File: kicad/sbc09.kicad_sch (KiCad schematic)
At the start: 78 parts, among them J1 Conn_01x03_Male, J2 Conn_01x06_Male, J3 Conn_01x06_Male, J4 Conn_01x06_Male, J5 Conn_02x05_Odd_Even, J6 Conn_02x25_Odd_Even, Q1 2N7000, SW1 SW_Push, U1 74LS245, U10 74LS670, U11 74LS670, U12 AS6C4008-55PCN, U13 SST39SF040-DIP, U14 SST39SF040-DIP, U15 XR68C681CJ, U16 MAX232, U2 74LS245, U3 74LS245, U4 MC6809E, U5 74HCT125, U6 ATF22V10C, U7 ATF22V10C, U8 74LS670, U9 74LS670, X1 8MHz, X2 3.6864MHz

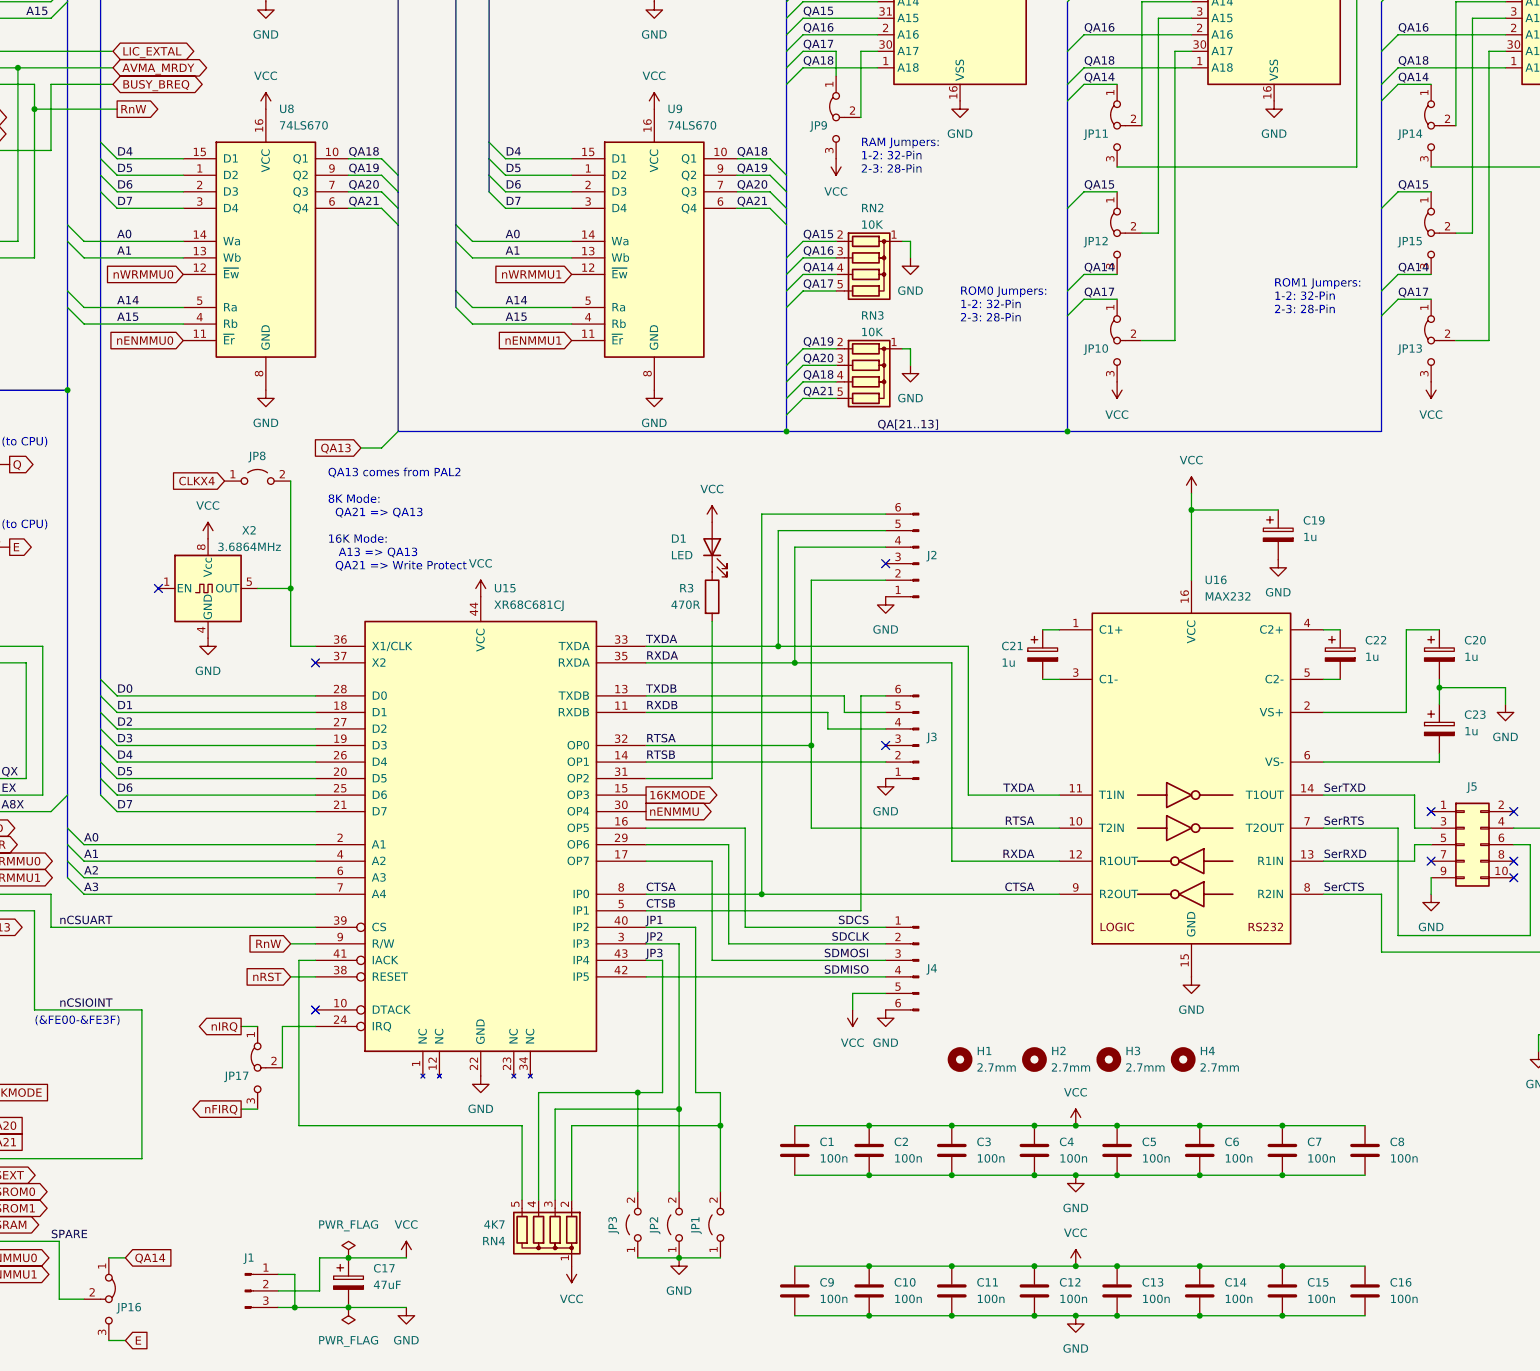
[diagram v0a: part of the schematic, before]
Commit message: Remove JP8 (caused fast clock stub) and renumbered remaining JPs
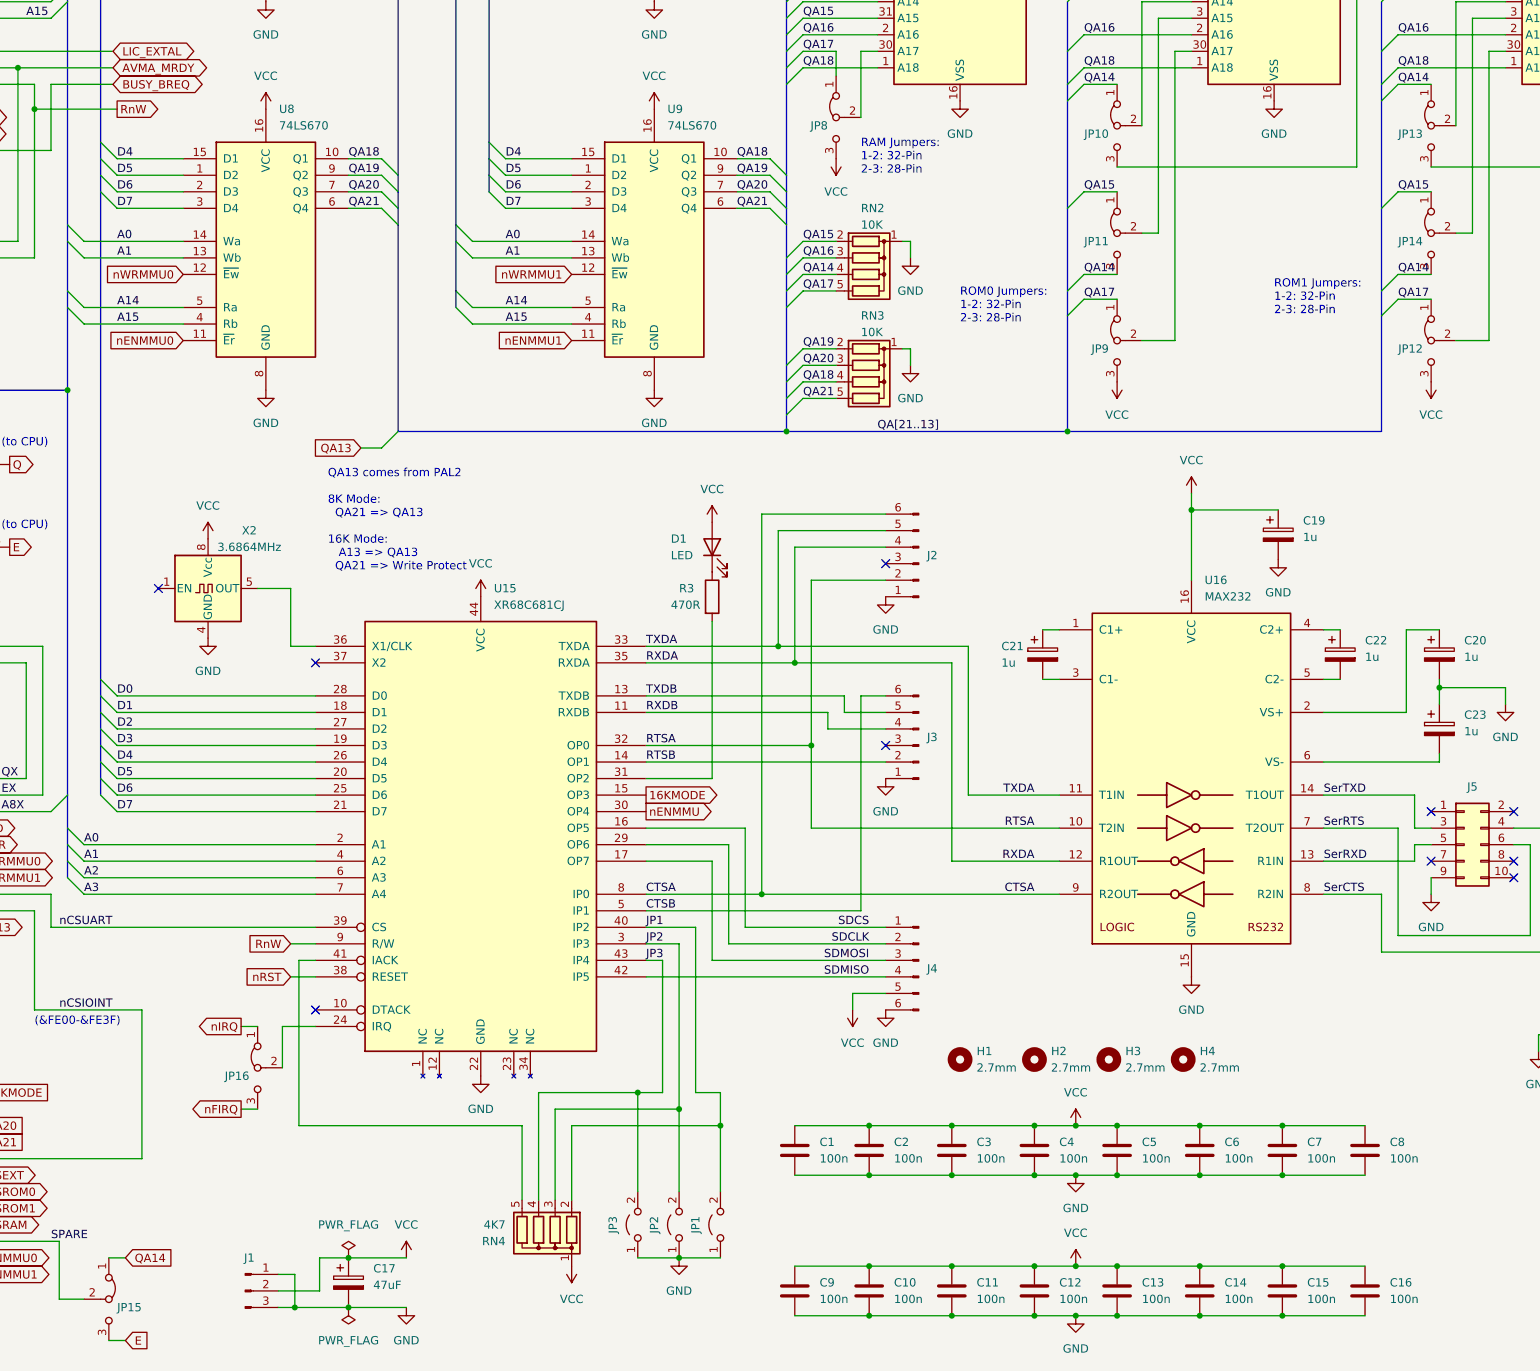
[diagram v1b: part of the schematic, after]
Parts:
- removed JP8: Jumper_2_Open, Connector_PinHeader_2.54mm:PinHeader_1x02_P2.54mm_Vertical, symbol Jumper:Jumper_2_Open
- renumbered JP11 to JP10, JP12 to JP11, JP13 to JP12, JP14 to JP13, JP15 to JP14, JP16 to JP15, JP17 to JP16, JP9 to JP8, JP10 to JP9
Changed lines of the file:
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@@
   (junction (at 134.62 269.24) (diameter 0) (color 0 0 0 0)
   )
-  (junction (at 125.73 166.37) (diameter 0) (color 0 0 0 0)
-  )
   (junction (at 289.56 71.12) (diameter 0) (color 0 0 0 0)
   )
@@
     (stroke (width 0) (type default) (color 0 0 0 0))
   )
-  (wire (pts (xy 125.73 149.86) (xy 125.73 166.37))
-    (stroke (width 0) (type default) (color 0 0 0 0))
-  )
   (wire (pts (xy 246.38 256.54) (xy 252.73 256.54))
     (stroke (width 0) (type default) (color 0 0 0 0))
@@
     )
   )
-  (global_label "CLKX4" (shape input) (at 115.57 149.86 180) (fields_autoplaced)
-    (effects (font (size 1.27 1.27)) (justify right))
-    (property "Intersheet References" "${INTERSHEET_REFS}" (id 0) (at 107.1698 149.7806 0)
-      (effects (font (size 1.27 1.27)) (justify right) hide)
-    )
-  )
   (global_label "nENMMU" (shape input) (at 46.99 243.84 180) (fields_autoplaced)
     (effects (font (size 1.27 1.27)) (justify right))
@@
   (symbol (lib_id "Jumper:Jumper_3_Bridged12") (at 300.99 128.27 90) (mirror x) (unit 1)
     (in_bom yes) (on_board yes)
-    (property "Reference" "JP13" (id 0) (at 299.72 129.54 90)
+    (property "Reference" "JP12" (id 0) (at 299.72 129.54 90)
       (effects (font (size 1.27 1.27)) (justify left))
     )
@@
     (pin "1")
   )
-  (symbol (lib_id "Jumper:Jumper_2_Open") (at 120.65 149.86 0) (unit 1)
-    (in_bom yes) (on_board yes) (fields_autoplaced)
-    (property "Reference" "JP8" (id 0) (at 120.65 146.05 0))
-    (property "Value" "Jumper_2_Open" (id 1) (at 120.65 146.05 0)
-      (effects (font (size 1.27 1.27)) hide)
-    )
-    (property "Footprint" "Connector_PinHeader_2.54mm:PinHeader_1x02_P2.54mm_Vertical" (id 2) (at 120.65 149.86 0)
-      (effects (font (size 1.27 1.27)) hide)
-    )
-    (property "Datasheet" "~" (id 3) (at 120.65 149.86 0)
-      (effects (font (size 1.27 1.27)) hide)
-    )
-    (pin "1")
-    (pin "2")
-  )
   (symbol (lib_id "power:VCC") (at 264.16 151.765 0) (unit 1)
     (in_bom yes) (on_board yes) (fields_autoplaced)
@@
   (symbol (lib_id "Jumper:Jumper_3_Bridged12") (at 97.79 275.59 270) (unit 1)
     (in_bom yes) (on_board yes)
-    (property "Reference" "JP16" (id 0) (at 99.06 276.86 90)
+    (property "Reference" "JP15" (id 0) (at 99.06 276.86 90)
       (effects (font (size 1.27 1.27)) (justify left))
     )
@@
   (symbol (lib_id "Jumper:Jumper_3_Bridged12") (at 209.55 93.98 90) (mirror x) (unit 1)
     (in_bom yes) (on_board yes)
-    (property "Reference" "JP9" (id 0) (at 208.28 95.25 90)
+    (property "Reference" "JP8" (id 0) (at 208.28 95.25 90)
       (effects (font (size 1.27 1.27)) (justify left))
     )
@@
   (symbol (lib_id "Jumper:Jumper_3_Bridged12") (at 300.99 95.25 90) (mirror x) (unit 1)
     (in_bom yes) (on_board yes)
-    (property "Reference" "JP14" (id 0) (at 299.72 96.52 90)
+    (property "Reference" "JP13" (id 0) (at 299.72 96.52 90)
       (effects (font (size 1.27 1.27)) (justify left))
     )
@@
   (symbol (lib_id "Jumper:Jumper_3_Bridged12") (at 300.99 111.76 90) (mirror x) (unit 1)
     (in_bom yes) (on_board yes)
-    (property "Reference" "JP15" (id 0) (at 299.72 113.03 90)
+    (property "Reference" "JP14" (id 0) (at 299.72 113.03 90)
       (effects (font (size 1.27 1.27)) (justify left))
     )
@@
   (symbol (lib_id "Jumper:Jumper_3_Bridged12") (at 120.65 240.03 90) (mirror x) (unit 1)
     (in_bom yes) (on_board yes)
-    (property "Reference" "JP17" (id 0) (at 119.38 241.3 90)
+    (property "Reference" "JP16" (id 0) (at 119.38 241.3 90)
       (effects (font (size 1.27 1.27)) (justify left))
     )
@@
   (symbol (lib_id "Jumper:Jumper_3_Bridged12") (at 252.73 111.76 90) (mirror x) (unit 1)
     (in_bom yes) (on_board yes)
-    (property "Reference" "JP12" (id 0) (at 251.46 113.03 90)
+    (property "Reference" "JP11" (id 0) (at 251.46 113.03 90)
       (effects (font (size 1.27 1.27)) (justify left))
     )
@@
   (symbol (lib_id "Jumper:Jumper_3_Bridged12") (at 252.73 128.27 90) (mirror x) (unit 1)
     (in_bom yes) (on_board yes)
-    (property "Reference" "JP10" (id 0) (at 251.46 129.54 90)
+    (property "Reference" "JP9" (id 0) (at 251.46 129.54 90)
       (effects (font (size 1.27 1.27)) (justify left))
     )
@@
   (symbol (lib_id "Jumper:Jumper_3_Bridged12") (at 252.73 95.25 90) (mirror x) (unit 1)
     (in_bom yes) (on_board yes)
-    (property "Reference" "JP11" (id 0) (at 251.46 96.52 90)
+    (property "Reference" "JP10" (id 0) (at 251.46 96.52 90)
       (effects (font (size 1.27 1.27)) (justify left))
     )
@@
       (reference "JP7") (unit 1) (value "Jumper_2_Open") (footprint "Connector_PinHeader_2.54mm:PinHeader_1x02_P2.54mm_Vertical")
     )
-    (path "/19991cde-5872-4534-b621-6cbf04dc9f4c"
-      (reference "JP8") (unit 1) (value "Jumper_2_Open") (footprint "Connector_PinHeader_2.54mm:PinHeader_1x02_P2.54mm_Vertical")
-    )
     (path "/7a4424d4-d9b6-473e-bf14-0d763552d25b"
-      (reference "JP9") (unit 1) (value "Jumper_3_Bridged12") (footprint "Connector_PinHeader_2.54mm:PinHeader_1x03_P2.54mm_Vertical")
+      (reference "JP8") (unit 1) (value "Jumper_3_Bridged12") (footprint "Connector_PinHeader_2.54mm:PinHeader_1x03_P2.54mm_Vertical")
     )
     (path "/db418079-65d1-4ede-8ef0-5b1cfbaf450d"
-      (reference "JP10") (unit 1) (value "Jumper_3_Bridged12") (footprint "Connector_PinHeader_2.54mm:PinHeader_1x03_P2.54mm_Vertical")
+      (reference "JP9") (unit 1) (value "Jumper_3_Bridged12") (footprint "Connector_PinHeader_2.54mm:PinHeader_1x03_P2.54mm_Vertical")
     )
     (path "/f28bf192-1a75-4e39-8997-6becaa19eea9"
-      (reference "JP11") (unit 1) (value "Jumper_3_Bridged12") (footprint "Connector_PinHeader_2.54mm:PinHeader_1x03_P2.54mm_Vertical")
+      (reference "JP10") (unit 1) (value "Jumper_3_Bridged12") (footprint "Connector_PinHeader_2.54mm:PinHeader_1x03_P2.54mm_Vertical")
     )
     (path "/d7680e53-0e0e-4b97-87ab-499c51605b34"
-      (reference "JP12") (unit 1) (value "Jumper_3_Bridged12") (footprint "Connector_PinHeader_2.54mm:PinHeader_1x03_P2.54mm_Vertical")
+      (reference "JP11") (unit 1) (value "Jumper_3_Bridged12") (footprint "Connector_PinHeader_2.54mm:PinHeader_1x03_P2.54mm_Vertical")
     )
     (path "/04e99d5a-3097-4481-9abd-c24e69c6a482"
-      (reference "JP13") (unit 1) (value "Jumper_3_Bridged12") (footprint "Connector_PinHeader_2.54mm:PinHeader_1x03_P2.54mm_Vertical")
+      (reference "JP12") (unit 1) (value "Jumper_3_Bridged12") (footprint "Connector_PinHeader_2.54mm:PinHeader_1x03_P2.54mm_Vertical")
     )
     (path "/84c34303-5906-4801-a7f7-4daf021de84e"
-      (reference "JP14") (unit 1) (value "Jumper_3_Bridged12") (footprint "Connector_PinHeader_2.54mm:PinHeader_1x03_P2.54mm_Vertical")
+      (reference "JP13") (unit 1) (value "Jumper_3_Bridged12") (footprint "Connector_PinHeader_2.54mm:PinHeader_1x03_P2.54mm_Vertical")
     )
     (path "/c73b7152-27ce-41bf-a5c1-4113b79fe2e7"
-      (reference "JP15") (unit 1) (value "Jumper_3_Bridged12") (footprint "Connector_PinHeader_2.54mm:PinHeader_1x03_P2.54mm_Vertical")
+      (reference "JP14") (unit 1) (value "Jumper_3_Bridged12") (footprint "Connector_PinHeader_2.54mm:PinHeader_1x03_P2.54mm_Vertical")
     )
     (path "/4641aecc-47b7-4dc3-a987-d904d86e9328"
-      (reference "JP16") (unit 1) (value "Jumper_3_Bridged12") (footprint "Connector_PinHeader_2.54mm:PinHeader_1x03_P2.54mm_Vertical")
+      (reference "JP15") (unit 1) (value "Jumper_3_Bridged12") (footprint "Connector_PinHeader_2.54mm:PinHeader_1x03_P2.54mm_Vertical")
     )
     (path "/cf0544d4-3c74-4380-9e0e-133d2f215538"
-      (reference "JP17") (unit 1) (value "Jumper_3_Bridged12") (footprint "Connector_PinHeader_2.54mm:PinHeader_1x03_P2.54mm_Vertical")
+      (reference "JP16") (unit 1) (value "Jumper_3_Bridged12") (footprint "Connector_PinHeader_2.54mm:PinHeader_1x03_P2.54mm_Vertical")
     )
     (path "/262aa419-0fa8-4016-95e2-b1df66d01220"
